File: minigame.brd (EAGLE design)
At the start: 98.7 x 80 mm, 40 parts, among them J1 AVR_SPI_PRG_6PTH, Q1 MMBT2222A, U1 MCP73831, U2 MIC5219 3.3V, Y1 8MHz

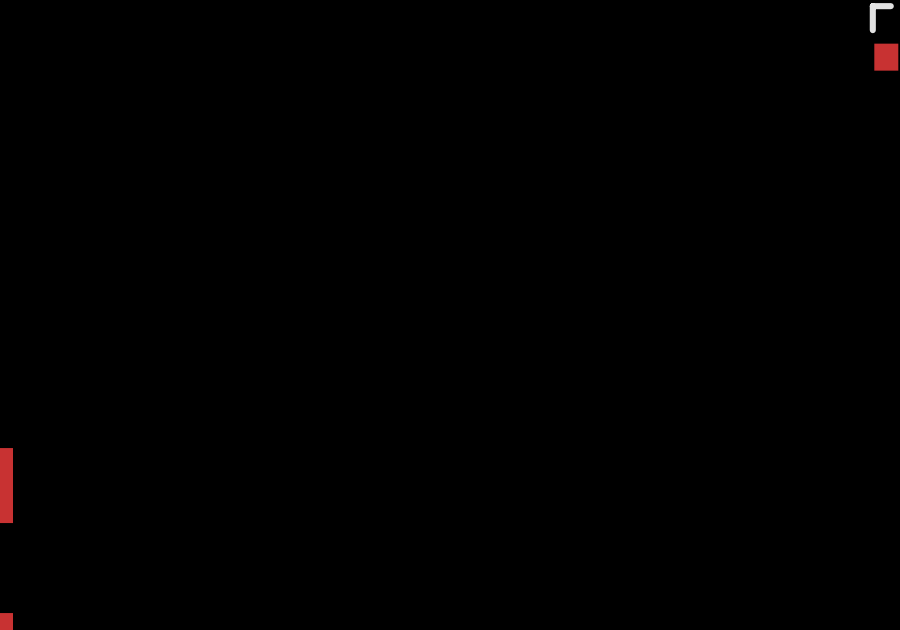
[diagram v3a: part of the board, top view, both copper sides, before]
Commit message: Added RX/TX LEDs
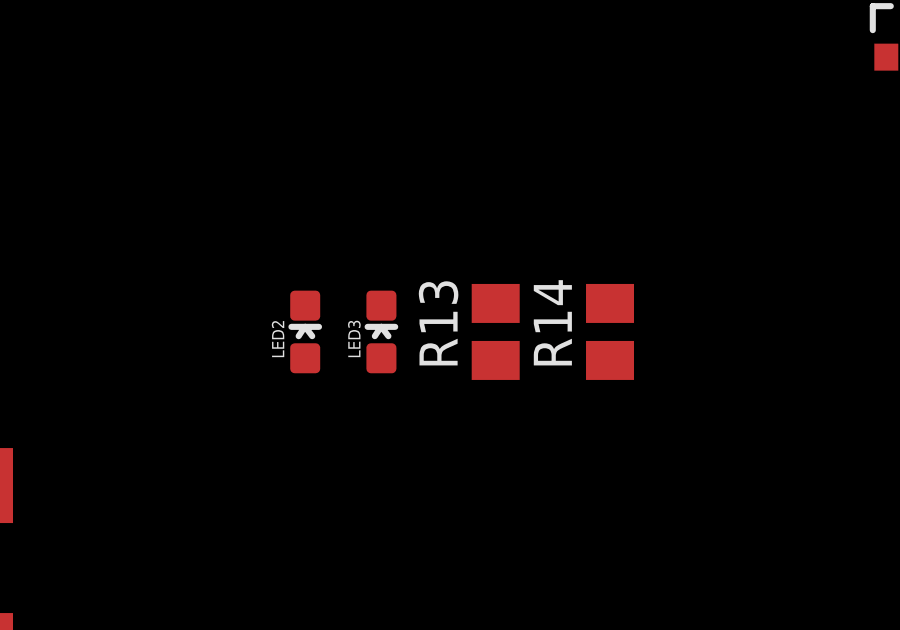
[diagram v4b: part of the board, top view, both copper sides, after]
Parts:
- added LED2: YELLOW, SparkFun-LED:LED-0603
- added LED3: BLUE, SparkFun-LED:LED-0603
- added R13, R14: 330, rcl:M0805
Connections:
- new net N$12: LED2.A, R13.2
- new net N$13: LED3.A, R14.2
- new net N$15: R13.1, U$1.22
- new net N$16: R14.1, U$1.8
- net GND: now also LED2.C, LED3.C
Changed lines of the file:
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@@
 </element>
 <element name="R12" library="rcl" package="M0805" value="180" x="90.17" y="22.86"/>
+<element name="LED2" library="SparkFun-LED" package="LED-0603" value="YELLOW" x="64.77" y="12.7"/>
+<element name="LED3" library="SparkFun-LED" package="LED-0603" value="BLUE" x="67.31" y="12.7"/>
+<element name="R13" library="rcl" package="M0805" value="330" x="71.12" y="12.7" rot="R90"/>
+<element name="R14" library="rcl" package="M0805" value="330" x="74.93" y="12.7" rot="R90"/>
 </elements>
 <signals>
@@
 <contactref element="OLED128X64" pad="8"/>
 <contactref element="Q1" pad="2"/>
+<contactref element="LED2" pad="C"/>
+<contactref element="LED3" pad="C"/>
 <wire x1="55.88" y1="68.58" x2="82.55" y2="66.04" width="0" layer="19" extent="16-16"/>
 <wire x1="50.19" y1="51.52" x2="55.88" y2="68.58" width="0" layer="19" extent="1-1"/>
@@
 <wire x1="6.03" y1="8.89" x2="3.95" y2="16.51" width="0" layer="19" extent="1-1"/>
 <wire x1="3.68" y1="30.48" x2="6.35" y2="22.8299" width="0" layer="19" extent="1-1"/>
+<wire x1="64.77" y1="13.577" x2="6.03" y2="8.89" width="0" layer="19" extent="1-1"/>
+<wire x1="67.31" y1="13.577" x2="64.77" y2="13.577" width="0" layer="19" extent="1-1"/>
 <wire x1="51.13" y1="7.58" x2="29.08" y2="10.16" width="0" layer="19" extent="1-1"/>
-<wire x1="86.04" y1="21.86" x2="6.03" y2="8.89" width="0" layer="19" extent="1-1"/>
 <wire x1="27.94" y1="74.93" x2="43.79" y2="51.52" width="0" layer="19" extent="1-1"/>
 <wire x1="15.11" y1="66.04" x2="27.94" y2="74.93" width="0" layer="19" extent="1-1"/>
@@
 <wire x1="15.11" y1="58.42" x2="15.11" y2="62.23" width="0" layer="19" extent="1-1"/>
 <wire x1="6.096" y1="76.835" x2="15.11" y2="66.04" width="0" layer="19" extent="1-1"/>
+<wire x1="86.04" y1="21.86" x2="51.13" y2="7.58" width="0" layer="19" extent="1-1"/>
 </signal>
 <signal name="3.3V">
@@
 <wire x1="91.12" y1="22.86" x2="47.79" y2="39.92" width="0" layer="19" extent="1-1"/>
 </signal>
+<signal name="N$12">
+<contactref element="R13" pad="2"/>
+<contactref element="LED2" pad="A"/>
+<wire x1="64.77" y1="11.823" x2="71.12" y2="13.65" width="0" layer="19" extent="1-1"/>
+</signal>
+<signal name="N$13">
+<contactref element="R14" pad="2"/>
+<contactref element="LED3" pad="A"/>
+<wire x1="67.31" y1="11.823" x2="74.93" y2="13.65" width="0" layer="19" extent="1-1"/>
+</signal>
+<signal name="N$15">
+<contactref element="U$1" pad="22"/>
+<contactref element="R13" pad="1"/>
+<wire x1="71.12" y1="11.75" x2="50.99" y2="39.92" width="0" layer="19" extent="1-1"/>
+</signal>
+<signal name="N$16">
+<contactref element="U$1" pad="8"/>
+<contactref element="R14" pad="1"/>
+<wire x1="74.93" y1="11.75" x2="41.19" y2="44.12" width="0" layer="19" extent="1-1"/>
+</signal>
 </signals>
